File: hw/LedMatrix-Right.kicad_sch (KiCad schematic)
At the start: 84 parts, among them Q1400 DTA114E, Q1401 DTA114E, Q1402 DTA114E, Q1403 DTA114E, Q1404 DTA114E, Q1405 DTA114E, Q1406 DTA114E, Q1407 DTA114E, Q1408 DTA114E, Q1409 DTC114EE, Q1410 DTC114EE, Q1411 DTC114EE, Q1412 DTC114EE, Q1413 DTC114EE, Q1414 DTC114EE, Q1415 DTC114EE, Q1416 DTC114EE, Q1417 DTC114EE, Q1418 DTC114EE, Q1419 DTC114EE, Q1420 DTC114EE, Q1421 DTC114EE, Q1422 DTC114EE, Q1423 DTC114EE, X1400 Lightpipe-5x5mm-Dome, X1401 Lightpipe-5x5mm-Dome, X1402 Lightpipe-5x5mm-Dome

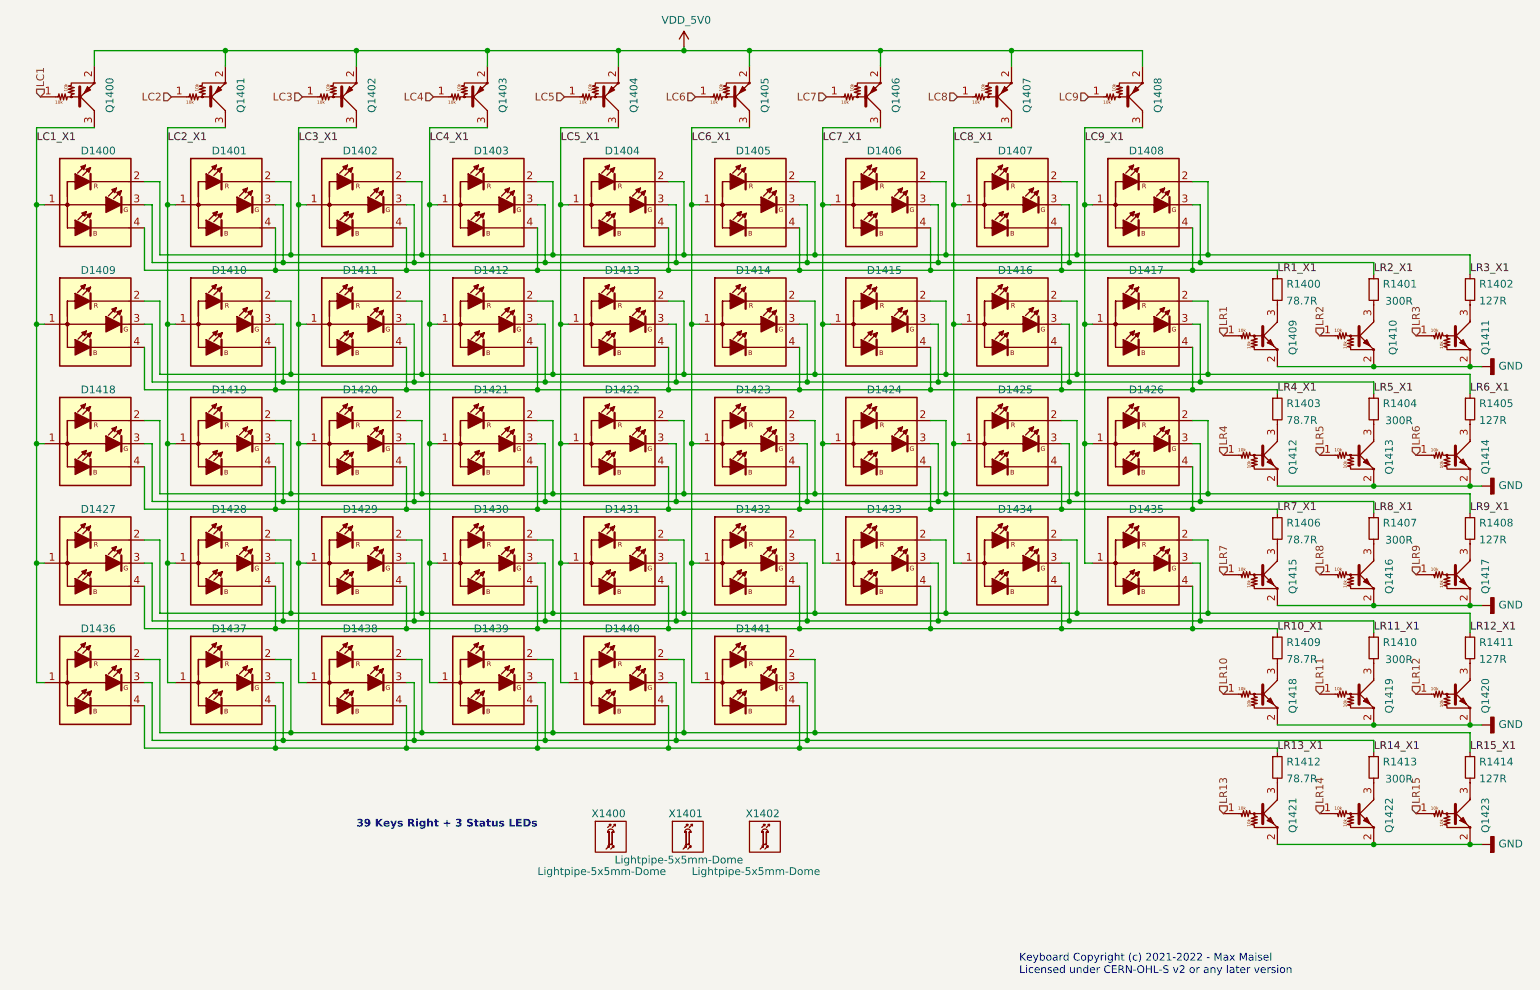
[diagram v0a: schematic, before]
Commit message: Replace LED matrix BJTs with MOSFETs and update PCB.
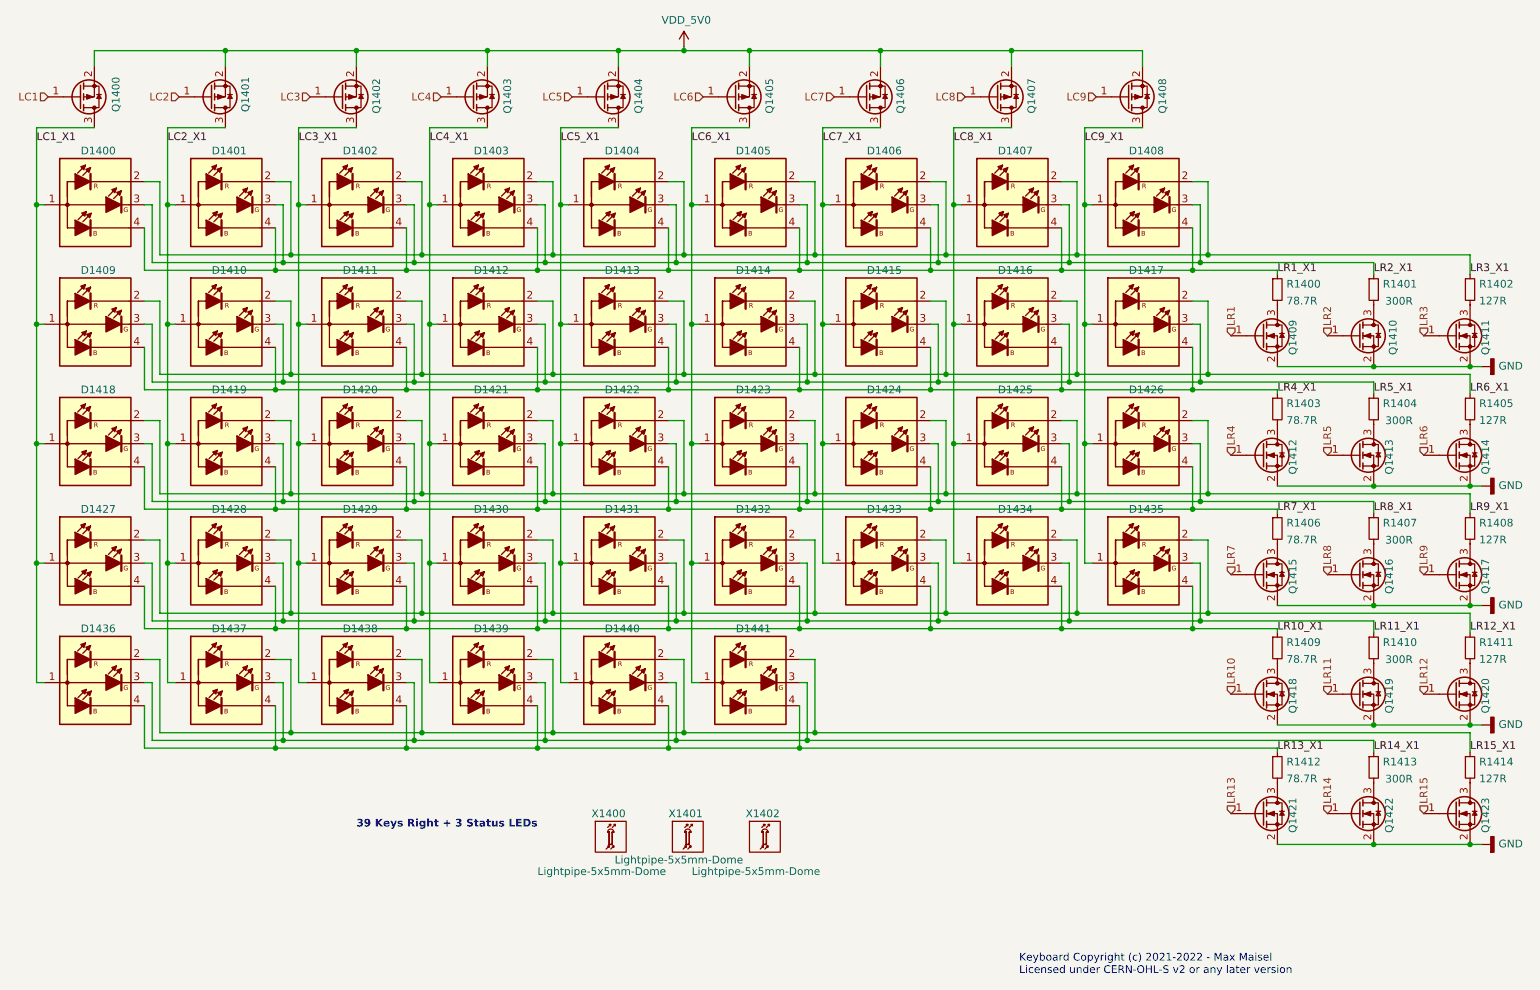
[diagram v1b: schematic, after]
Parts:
- Q1400, Q1401, Q1402, Q1403, Q1404, Q1405, Q1406, Q1407, Q1408: value DTA114E -> NTA4151P; symbol Keyboard:DTA114E -> Keyboard:NTA4151PT1G; farnell# (none) -> 2317622; mouser# (none) -> 863-NTA4151PT1G
- Q1409, Q1410, Q1411, Q1412, Q1413, Q1414, Q1415, Q1416, Q1417, Q1418, Q1419, Q1420, Q1421, Q1422, Q1423: value DTC114EE -> NTA4153N; symbol Keyboard:DTC114EE -> Keyboard:NTA4153NT1G; farnell# (none) -> 2317621; mouser# 863-DTC114EET1G -> 863-NTA4153NT1G
